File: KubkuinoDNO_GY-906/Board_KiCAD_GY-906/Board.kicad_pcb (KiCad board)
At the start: 2 copper layers, 33 parts, among them J1 Piezo, J2 AC/DC In (12V), J3 Prog, J4 Czujnik, J6 LCD, J7 Button, J8 Bluetooth, Q1 S8050, SW1 Reset, U1 LM7805_TO220, U2 ATMEGA328P-PU, Y1 Crystal

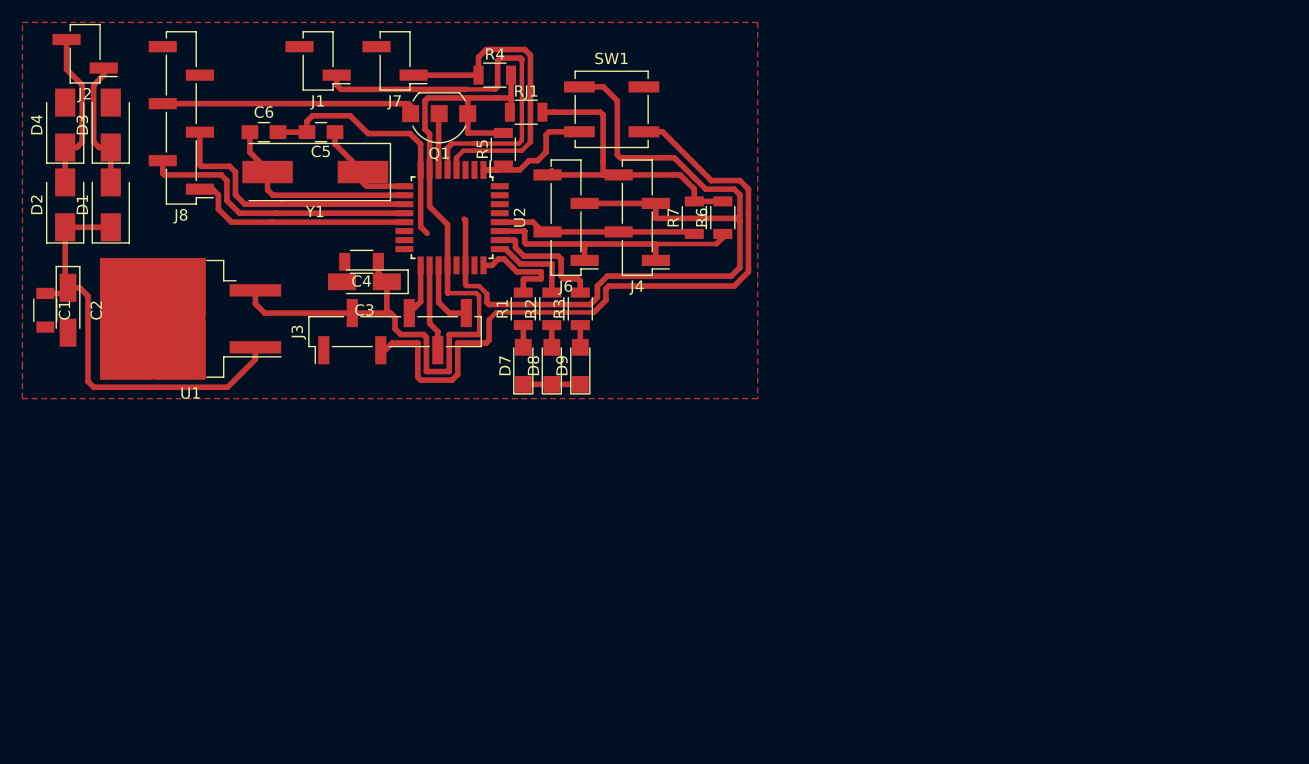
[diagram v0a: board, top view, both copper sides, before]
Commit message: Fixed SMD board
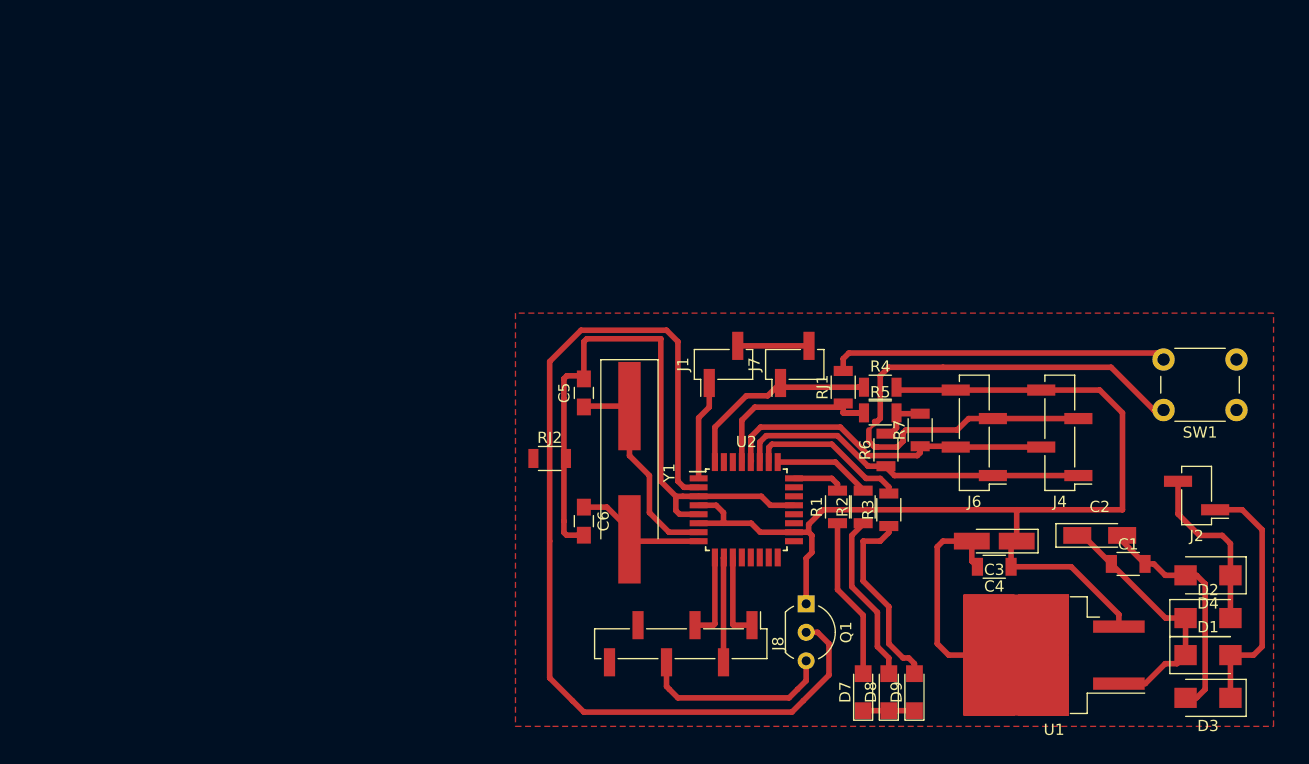
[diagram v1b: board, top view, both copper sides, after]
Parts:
- removed J3: Prog, Pin_Headers:Pin_Header_Straight_1x06_Pitch2.54mm_SMD_Pin1Left
- added RJ2: 0, Resistors_SMD:R_1206, F.Cu at (118.1, 89.2)
- SW1: footprint Buttons_Switches_SMD:SW_SPST_B3SL-1002P -> Buttons_Switches_THT:SW_PUSH_6mm_h5mm
- U2: value ATMEGA328P-PU -> ATMEGA328P-AU
- Y1: footprint Crystals:Crystal_SMD_HC49-SD -> Crystals:Crystal_SMD_HC49-SD_HandSoldering
- moved D3 110.3 mm to (176.8, 110.5), turned to 180 degrees
- moved D4 109.5 mm to (176.8, 99.6), turned to 180 degrees
- moved D2 108.3 mm to (176.8, 103.4), turned to 0 degrees
- moved J2 106.6 mm to (175.8, 92.5)
- moved D1 105.7 mm to (176.8, 106.7), turned to 0 degrees
- moved C1 99.1 mm to (169.7, 98.6), turned to 0 degrees
- moved C2 94.1 mm to (167.1, 96.0), turned to 0 degrees
- moved U1 82.6 mm to (163.1, 106.7)
- moved J8 64.6 mm to (129.8, 105.7), turned to 270 degrees
- moved C4 62.6 mm to (157.7, 98.8)
- moved SW1 61.8 mm to (179.3, 84.8), turned to 180 degrees
- moved C3 60.7 mm to (157.7, 96.5)
- moved Q1 53.1 mm to (141.0, 102.1), turned to 270 degrees
- moved J1 45.1 mm to (133.6, 80.8), turned to 90 degrees
- moved C6 44.9 mm to (121.2, 94.7), turned to 270 degrees
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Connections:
- RJ1 pad 1: 5V -> Reset
- RJ1 pad 2: 5V -> Net-(RJ1-Pad2)
- SW1 pad 2: Reset -> Net-(RJ1-Pad2)
- U2 pad 1: Reset -> Net-(J1-Pad1)
- U2 pad 10: xtal2 -> Brx
- U2 pad 11: Btx -> Bkey
- U2 pad 12: Brx -> (no net)
- U2 pad 13: Bkey -> (no net)
- U2 pad 15: (no net) -> Net-(J3-Pad4)
- U2 pad 16: (no net) -> Net-(J3-Pad5)
- U2 pad 18: Net-(J3-Pad5) -> 5V
- U2 pad 19: Net-(J3-Pad6) (its old number) -> (no net)
- U2 pad 2: (no net) -> BT
- U2 pad 20: 5V -> (no net)
- U2 pad 21: (no net) -> GND
- U2 pad 22: GND -> (no net)
- U2 pad 29: (no net) -> Reset
- U2 pad 3: (no net) -> GND
- U2 pad 32: (no net) -> Button
- U2 pad 4: Button -> 5V
- U2 pad 5: Net-(J1-Pad1) -> GND
- U2 pad 6: BT -> 5V
- U2 pad 7: 5V -> xtal1
- U2 pad 8: GND -> xtal2
- U2 pad 9: xtal1 -> Btx
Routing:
- net BT: track 4.67 -> 88.5 mm
- net GND: track 104.8 -> 165.0 mm
- net Reset: track 75.1 -> 17.4 mm
- net Net-(RJ1-Pad2): track 0.00 -> 30.1 mm
- net Net-(J1-Pad1): track 36.2 -> 8.89 mm
- net Btx: track 23.8 -> 7.74 mm
- net Brx: track 25.2 -> 9.40 mm
- net Net-(C1-Pad1): track 38.7 -> 23.0 mm
- net Net-(D9-Pad2): track 1.98 -> 17.2 mm
- net Net-(D8-Pad2): track 1.98 -> 15.2 mm
- net SCL: track 17.8 -> 30.5 mm
- net Bkey: track 20.3 -> 7.71 mm
- net Net-(D7-Pad2): track 1.98 -> 14.4 mm
- net Net-(D1-Pad2): track 11.8 -> 22.3 mm
- net Button: track 28.5 -> 18.2 mm
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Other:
- rule pad_to_mask_clearance: 0.2 -> 0

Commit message: Finished PCB
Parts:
- removed RJ2: 0, Resistors_SMD:R_1206
- added J3: Prog, Pin_Headers:Pin_Header_Straight_2x03_Pitch2.54mm, F.Cu at (119.9, 104.6)
- moved C1 9.64 mm to (166.6, 107.7), turned to 270 degrees
- moved C3 6.90 mm to (150.9, 95.8), turned to 270 degrees
- moved SW1 6.06 mm to (176.0, 79.8), turned to 270 degrees
- moved C4 5.79 mm to (153.2, 95.2), turned to 270 degrees
- moved C2 5.36 mm to (166.6, 101.3), turned to 270 degrees
- moved U1 4.85 mm to (159.5, 103.4), turned to 270 degrees
- moved D2 3.78 mm to (173.2, 102.1)
- moved D3 3.78 mm to (173.2, 109.2)
- moved D1 3.70 mm to (173.2, 105.7)
- moved D4 3.64 mm to (173.2, 98.8)
- moved J2 2.34 mm to (173.5, 93.0), turned to 270 degrees
- moved J1 0.80 mm to (133.9, 81.5)
- moved J7 0.76 mm to (140.0, 81.5)
- moved R6 0.25 mm to (148.3, 88.4)
- moved RJ1 0.25 mm to (144.3, 83.1)
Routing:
- net Net-(J3-Pad4): track 0.00 -> 49.3 mm, vias 0 -> 1
- net Reset: track 17.4 -> 43.8 mm, vias 0 -> 1
- net GND: track 165.0 -> 139.8 mm, vias 0 -> 2
- net Net-(J3-Pad1): track 0.00 -> 24.5 mm, vias 0 -> 1
- net Net-(J3-Pad3): track 0.00 -> 24.3 mm, vias 0 -> 1
- net 5V: track 101.7 -> 117.8 mm, vias 0 -> 1
- net Net-(RJ1-Pad2): track 30.1 -> 35.3 mm
- net Net-(D2-Pad2): track 15.3 -> 10.5 mm
- net Net-(D1-Pad2): track 22.3 -> 20.0 mm
- net Button: track 18.2 -> 20.3 mm
- net BT: track 88.5 -> 90.5 mm
- net Net-(J1-Pad1): track 8.89 -> 8.23 mm
- added copper zone on B.Cu, net GND
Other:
- net class Default: trace_width 0.5 -> 0.45
- net class Dolne added: clearance 0.2, trace_width 0.6, via_dia 0.6, via_drill 0.4
- board text added: "D1-D4"

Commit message: Update
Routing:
- net Net-(J3-Pad4): track 49.3 -> 61.6 mm
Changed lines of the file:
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@@
-(kicad_pcb (version 4) (host pcbnew 4.0.7)
+(kicad_pcb (version 4) (host pcbnew 4.0.6)
   (general
     (links 79)
-    (no_connects 10)
+    (no_connects 0)
     (area 115.062 76.2 182.626001 113.030001)
     (thickness 1.6)
     (drawings 1)
-    (tracks 293)
+    (tracks 294)
     (zones 0)
     (modules 33)
@@
   (segment (start 135.236 89.476) (end 135.236 87.122) (width 0.45) (layer F.Cu) (net 12))
   (segment (start 144.272 85.09) (end 144.272 84.508) (width 0.45) (layer F.Cu) (net 12))
+  (segment (start 138.938 107.696) (end 138.938 109.982) (width 0.6) (layer B.Cu) (net 13))
+  (segment (start 117.348 107.696) (end 115.824 106.172) (width 0.6) (layer B.Cu) (net 13))
+  (segment (start 138.938 107.696) (end 117.348 107.696) (width 0.6) (layer B.Cu) (net 13))
+  (segment (start 117.094 102.108) (end 115.824 103.378) (width 0.6) (layer B.Cu) (net 13))
   (segment (start 115.824 103.378) (end 115.824 106.172) (width 0.6) (layer B.Cu) (net 13))
-  (segment (start 117.094 102.108) (end 115.824 103.378) (width 0.6) (layer B.Cu) (net 13))
-  (segment (start 139.954 108.712) (end 138.938 107.696) (width 0.6) (layer B.Cu) (net 13))
-  (segment (start 138.938 107.696) (end 117.348 107.696) (width 0.6) (layer B.Cu) (net 13))
-  (segment (start 117.348 107.696) (end 115.824 106.172) (width 0.6) (layer B.Cu) (net 13))
-  (segment (start 141.478 108.712) (end 142.748 107.442) (width 0.6) (layer B.Cu) (net 13))
-  (segment (start 142.748 107.442) (end 142.748 100.33) (width 0.6) (layer B.Cu) (net 13))
-  (segment (start 142.748 100.33) (end 141.478 99.06) (width 0.6) (layer B.Cu) (net 13))
-  (segment (start 141.478 99.06) (end 139.192 99.06) (width 0.6) (layer B.Cu) (net 13))
-  (segment (start 139.192 99.06) (end 137.668 100.584) (width 0.6) (layer B.Cu) (net 13))
-  (segment (start 141.478 108.712) (end 139.954 108.712) (width 0.6) (layer B.Cu) (net 13))
+  (segment (start 137.636 99.79) (end 137.636 97.976) (width 0.6) (layer F.Cu) (net 13) (status 800000))
+  (segment (start 137.668 99.822) (end 137.636 99.79) (width 0.6) (layer F.Cu) (net 13))
+  (via (at 137.668 99.822) (size 0.6) (drill 0.4) (layers F.Cu B.Cu) (net 13))
+  (segment (start 137.668 100.076) (end 137.668 99.822) (width 0.6) (layer B.Cu) (net 13))
+  (segment (start 137.668 96.266) (end 137.668 100.076) (width 0.6) (layer B.Cu) (net 13))
+  (segment (start 143.764 96.266) (end 137.668 96.266) (width 0.6) (layer B.Cu) (net 13))
+  (segment (start 144.018 96.52) (end 143.764 96.266) (width 0.6) (layer B.Cu) (net 13))
+  (segment (start 144.018 109.728) (end 144.018 96.52) (width 0.6) (layer B.Cu) (net 13))
+  (segment (start 143.764 109.982) (end 144.018 109.728) (width 0.6) (layer B.Cu) (net 13))
+  (segment (start 138.938 109.982) (end 143.764 109.982) (width 0.6) (layer B.Cu) (net 13))
   (segment (start 117.348 102.108) (end 117.094 102.108) (width 0.6) (layer B.Cu) (net 13))
-  (via (at 137.668 100.584) (size 0.6) (drill 0.4) (layers F.Cu B.Cu) (net 13))
-  (segment (start 137.668 100.584) (end 137.636 100.552) (width 0.6) (layer F.Cu) (net 13))
-  (segment (start 137.636 100.552) (end 137.636 97.976) (width 0.6) (layer F.Cu) (net 13))
   (segment (start 148.336 89.842) (end 149.278 89.842) (width 0.45) (layer F.Cu) (net 14))
   (segment (start 150.114 90.678) (end 157.611 90.678) (width 0.45) (layer F.Cu) (net 14))
@@
     (connect_pads (clearance 0.45))
     (min_thickness 0.1)
-    (fill (arc_segments 32) (thermal_gap 0.508) (thermal_bridge_width 0.508) (smoothing fillet))
+    (fill yes (arc_segments 32) (thermal_gap 0.508) (thermal_bridge_width 0.508) (smoothing fillet))
     (polygon
       (pts
@@
     (connect_pads (clearance 0.45))
     (min_thickness 0.1)
-    (fill (arc_segments 32) (thermal_gap 0.508) (thermal_bridge_width 0.508) (smoothing fillet))
+    (fill yes (arc_segments 32) (thermal_gap 0.508) (thermal_bridge_width 0.508) (smoothing fillet))
     (polygon
       (pts

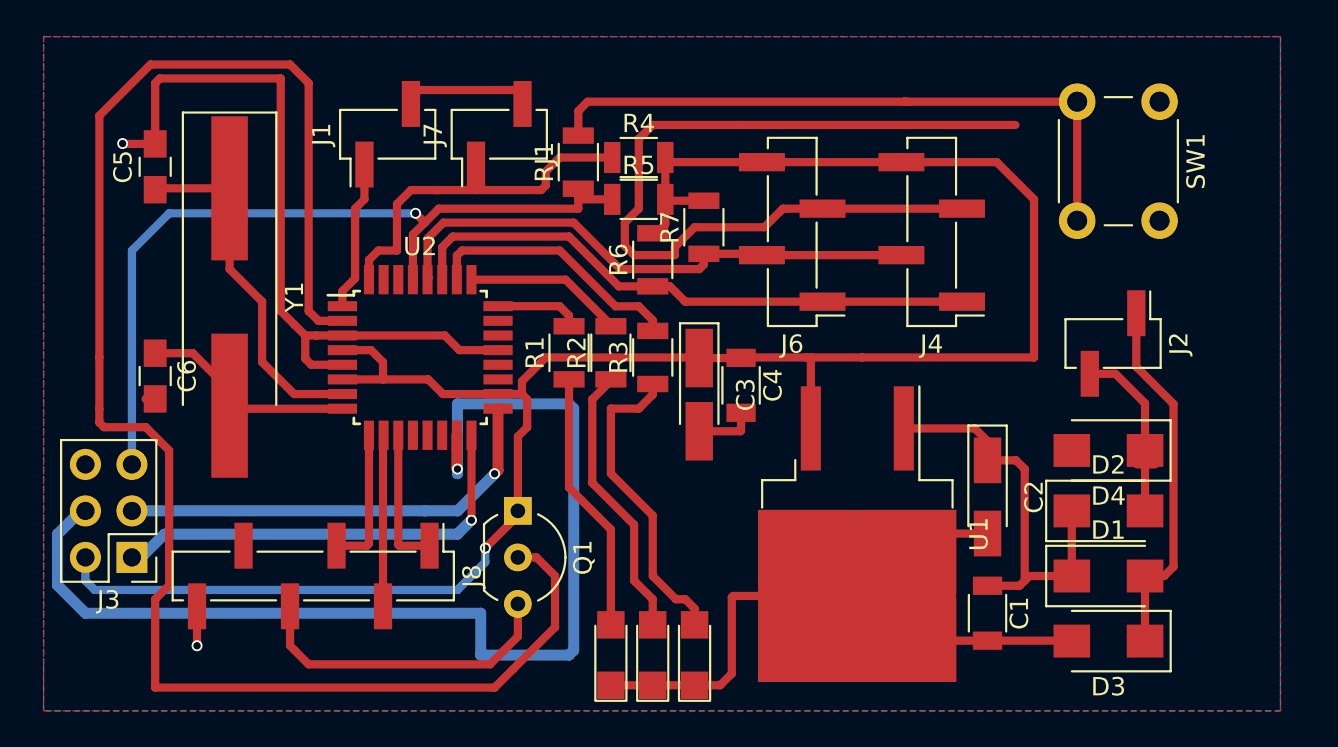
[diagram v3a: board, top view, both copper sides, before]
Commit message: Minor optimization
Board GY906:
Removed ICSP header and replaced with pads
Moved power input to the edge
Added fuse after LM7805

GY906 sketch:
Alarm has got new launch method (removed booleans)
Removed unused headers
Selected one tone frequency for buzzer
Some other things
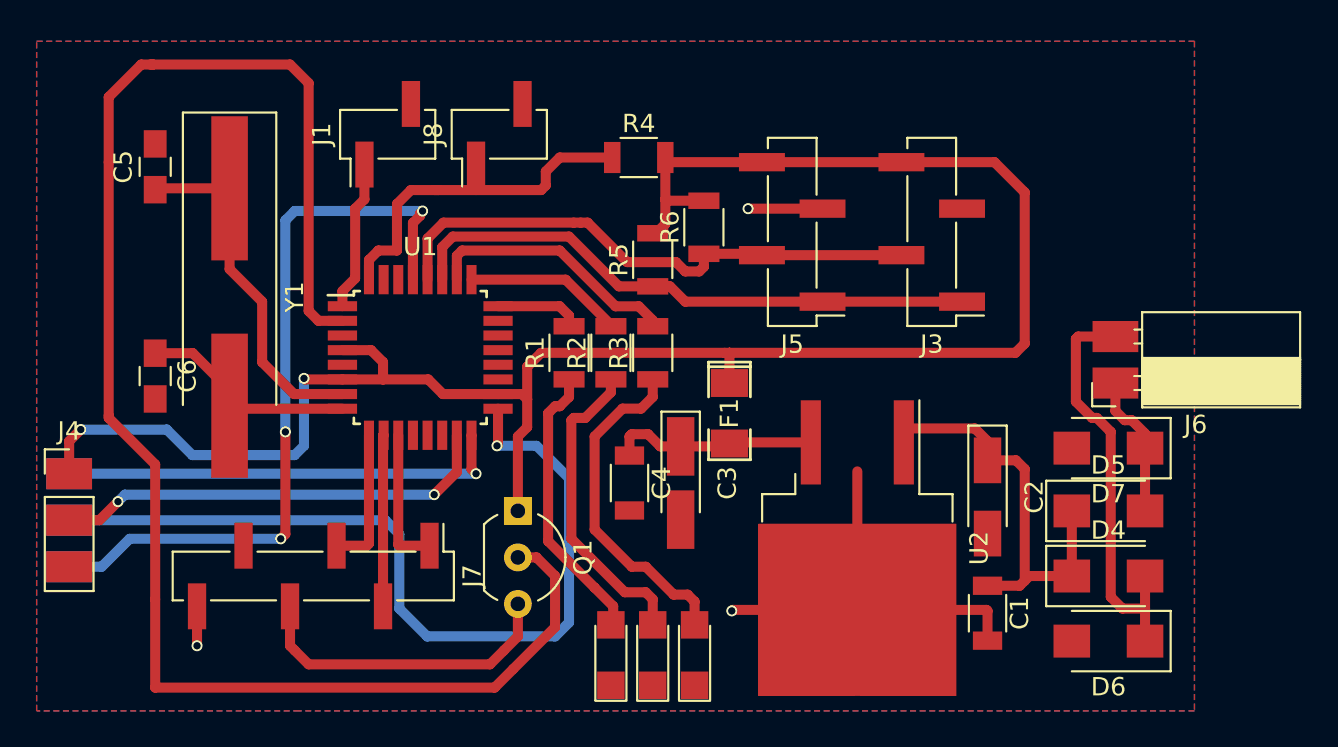
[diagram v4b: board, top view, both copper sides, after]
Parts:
- removed the J3 at (119.9, 104.6)
- removed the R5 at (147.6, 85.1)
- removed RJ1: 0, Resistors_SMD:R_1206
- removed SW1: Reset, Buttons_Switches_THT:SW_PUSH_6mm_h5mm
- added F1: 500mA 6V, SMD_Packages:SMD-1206_Pol, F.Cu at (152.5, 96.8)
- added J4: Conn_01x03, Socket_Strips:Socket_Strip_Straight_1x03_Pitch2.54mm, F.Cu at (116.5, 100.1)
- added J6: AC/DC In (12V), Socket_Strips:Socket_Strip_Angled_1x02_Pitch2.54mm, F.Cu at (173.6, 95.1)
- J2: value AC/DC In (12V) -> Conn_01x03; footprint Pin_Headers:Pin_Header_Straight_1x02_Pitch2.54mm_SMD_Pin1Left -> Socket_Strips:Socket_Strip_Straight_1x03_Pitch2.54mm; moved to B.Cu
- moved J2 57.5 mm to (116.5, 100.1), turned to 180 degrees
- moved C4 8.10 mm to (147.1, 100.6)
- moved C3 4.93 mm to (149.9, 100.6)
- moved U2 0.76 mm to (159.5, 104.1)
- moved R3 0.25 mm to (148.3, 93.5)
- moved D7 0.13 mm to (173.2, 98.7)
- renumbered D7 to D1, D8 to D2, D9 to D3, D1 to D4, D2 to D5, D3 to D6, D4 to D7, J4 to J3, J6 to J5, J8 to J7, J7 to J8, R6 to R5, R7 to R6, U2 to U1, U1 to U2
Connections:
- C3 pad 1: 5V -> Net-(C3-Pad1)
- C4 pad 1: 5V -> Net-(C3-Pad1)
- D4 pad 2: Net-(D1-Pad2) (its old number) -> Net-(D4-Pad2)
- D5 pad 2: Net-(D2-Pad2) (its old number) -> Net-(D5-Pad2)
- D6 pad 1: Net-(D1-Pad2) (its old number) -> Net-(D4-Pad2)
- D7 pad 1: Net-(D2-Pad2) (its old number) -> Net-(D5-Pad2)
- J2 pad 1: Net-(D1-Pad2) (its old number) -> Net-(J2-Pad1)
- J2 pad 2: Net-(D2-Pad2) (its old number) -> Net-(J2-Pad2)
- J7 pad 5: (no net) -> Net-(J7-Pad5)
- U1 pad 12: (no net) -> 1W
- U1 pad 13: (no net) -> Net-(U1-Pad13)
- U1 pad 14: (no net) -> Net-(U1-Pad14)
- U1 pad 16: Net-(J3-Pad1) -> Net-(J2-Pad1)
- U1 pad 17: Net-(J3-Pad3) -> Net-(J2-Pad2)
- U1 pad 19: (no net) -> Net-(U1-Pad19)
- U1 pad 20: (no net) -> Net-(U1-Pad20)
- U1 pad 22: (no net) -> Net-(U1-Pad22)
- U1 pad 23: (no net) -> Net-(U1-Pad23)
- U1 pad 30: (no net) -> Net-(U1-Pad30)
- U1 pad 31: (no net) -> Net-(U1-Pad31)
- U2 pad 3: 5V -> Net-(C3-Pad1)
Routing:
- net GND: track 139.8 -> 29.9 mm, vias 2 -> 3
- net Net-(J2-Pad2): track 0.00 -> 47.2 mm, vias 0 -> 1
- net Net-(J4-Pad2): track 61.6 -> 24.3 mm, vias 1 -> 2
- net Net-(RJ1-Pad2): track 35.3 -> 0.00 mm
- net Net-(J3-Pad1): track 24.5 -> 0.00 mm, vias 1 -> 0
- net Net-(J2-Pad1): track 0.00 -> 24.4 mm, vias 0 -> 1
- net Net-(J3-Pad3): track 24.3 -> 0.00 mm, vias 1 -> 0
- net Net-(D4-Pad2): track 0.00 -> 22.9 mm
- net Net-(D1-Pad2) (its old number): track 20.0 -> 0.00 mm
- net Net-(C3-Pad1): track 0.00 -> 11.4 mm
- net Net-(D2-Pad2) (its old number): track 10.5 -> 0.00 mm
- net 5V: track 117.8 -> 109.2 mm, vias 1 -> 2
- net Net-(D5-Pad2): track 0.00 -> 7.88 mm
- net Reset: track 43.8 -> 41.4 mm, vias 1 -> 3
- net Net-(D2-Pad2): track 15.2 -> 17.3 mm
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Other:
- net class Default: trace_width 0.45 -> 0.55
- net class Dolne: trace_width 0.6 -> 0.65

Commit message: Updates
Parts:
- removed J5: LCD, Pin_Headers:Pin_Header_Straight_1x04_Pitch2.54mm_SMD_Pin1Left
- J3: value Czujnik -> I2C; footprint Pin_Headers:Pin_Header_Straight_1x04_Pitch2.54mm_SMD_Pin1Left -> Socket_Strips:Socket_Strip_Straight_2x04_Pitch2.54mm_SMD
- moved D7 17.5 mm to (166.4, 82.5)
- moved D4 17.5 mm to (166.4, 89.6)
- moved D5 17.5 mm to (166.4, 86.0)
- moved D6 17.5 mm to (166.4, 93.2)
- moved J3 9.27 mm to (154.6, 84.7)
- moved J6 6.21 mm to (172.4, 89.0)
- moved R6 5.29 mm to (148.1, 82.3)
- moved R5 5.16 mm to (152.4, 91.6), turned to 180 degrees
- moved R4 2.09 mm to (145.5, 82.3), turned to 90 degrees
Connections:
- J3 pad 2: SCL -> SDA
- J3 pad 3: GND -> SCL
- J3 pad 4: 5V -> SCL
- J6 pad 1: Net-(D5-Pad2) -> Net-(D4-Pad2)
- J6 pad 2: Net-(D4-Pad2) -> Net-(D5-Pad2)
- J7 pad 5: Net-(J7-Pad5) -> (no net)
- U1 pad 12: 1W -> (no net)
- U1 pad 13: Net-(U1-Pad13) -> (no net)
- U1 pad 14: Net-(U1-Pad14) -> (no net)
- U1 pad 19: Net-(U1-Pad19) -> (no net)
- U1 pad 20: Net-(U1-Pad20) -> (no net)
- U1 pad 22: Net-(U1-Pad22) -> (no net)
- U1 pad 23: Net-(U1-Pad23) -> (no net)
- U1 pad 30: Net-(U1-Pad30) -> (no net)
- U1 pad 31: Net-(U1-Pad31) -> (no net)
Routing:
- net GND: track 29.9 -> 45.5 mm
- net 5V: track 109.2 -> 94.0 mm
- net Net-(D4-Pad2): track 22.9 -> 7.83 mm
- net Net-(C1-Pad1): track 22.6 -> 29.7 mm
- net SCL: track 30.7 -> 26.4 mm
- net SDA: track 32.0 -> 32.9 mm
- net Button: track 20.3 -> 19.4 mm
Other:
- net class Default: trace_width 0.55 -> 0.6
- net class Dolne: trace_width 0.65 -> 0.7
